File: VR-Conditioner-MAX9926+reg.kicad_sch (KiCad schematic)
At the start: 26 parts, among them J2 Edge, J3 8-pin header, U1 MAX9926UAEE+, U2 AMS1117CD-5.0

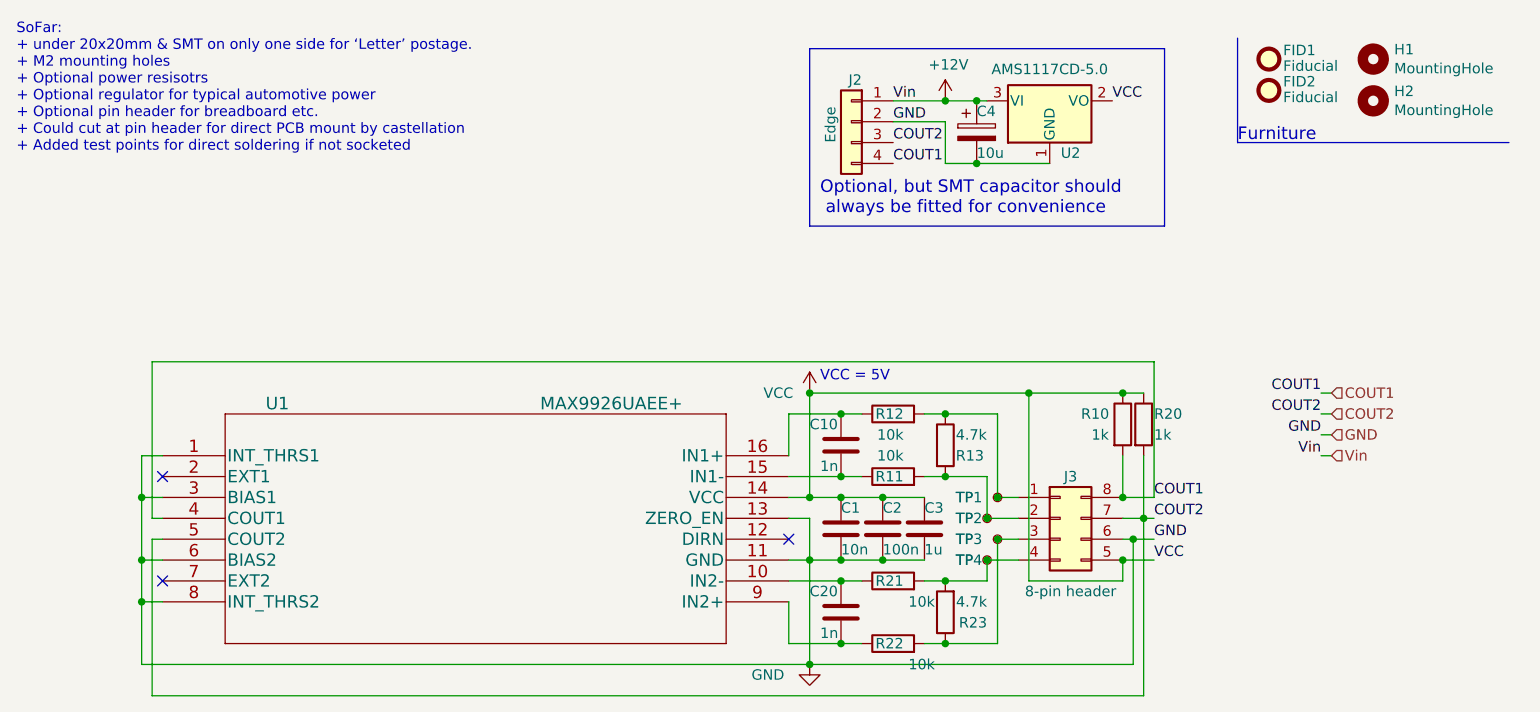
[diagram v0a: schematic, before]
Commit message: v3.74 corrects channel 1 polarity, improves silkscreen & makes soldering of PTH bits easier.
Polarity in previous version not critical as everyone seems to try their pick-up each way anyhow.
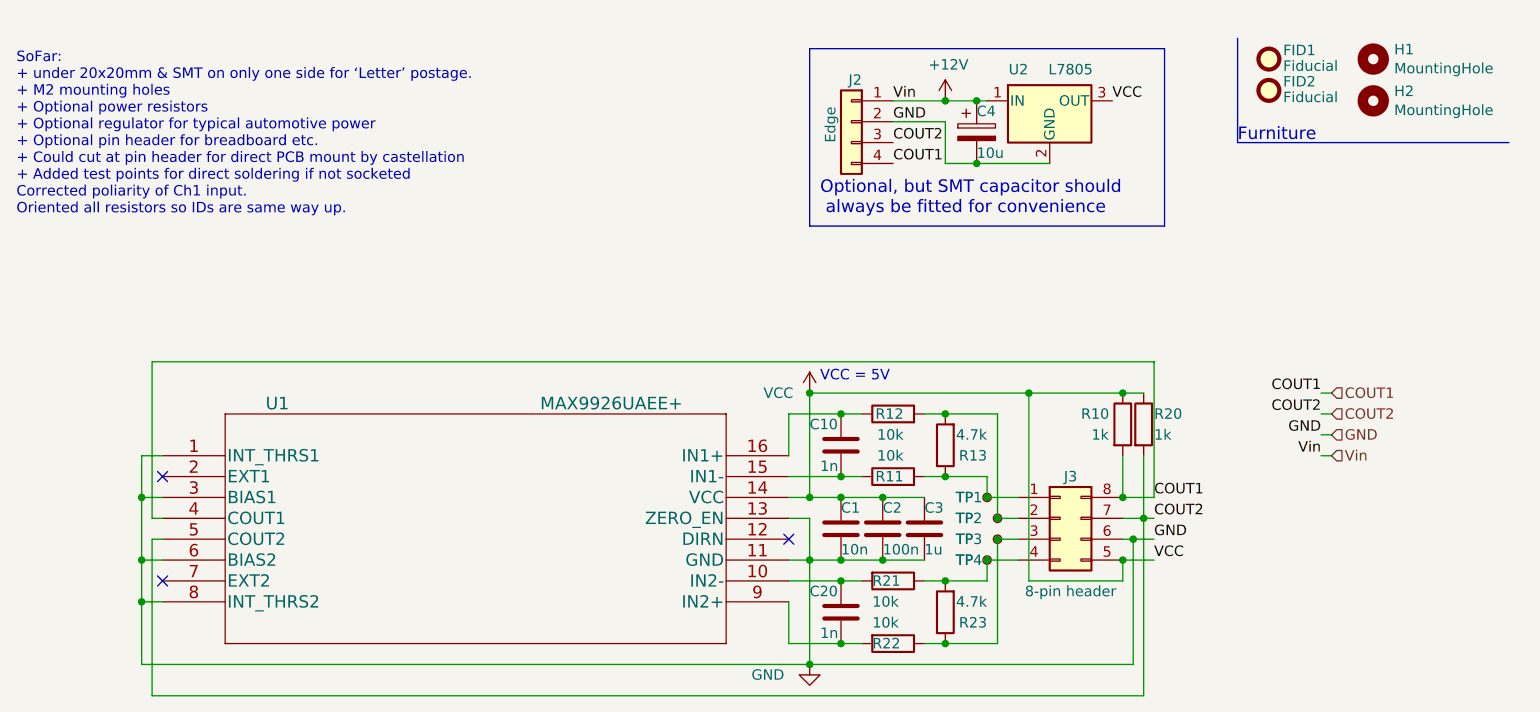
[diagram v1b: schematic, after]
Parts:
- removed U2: AMS1117CD-5.0, Package_TO_SOT_THT:TO-92_Inline_Wide, symbol Regulator_Linear:AMS1117CD-5.0
- added U2: L7805, Package_TO_SOT_THT:TO-220-3_Vertical, symbol Regulator_Linear:L7805
- R11, R12, R21, R22: footprint Resistor_SMD:R_1206_3216Metric -> Resistor_SMD:R_1206_3216Metric_Pad1.30x1.75mm_HandSolder
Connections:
- net +12V: now also U2.1 (IN)
- net GND: now also U2.2 (GND)
- net VCC: now also U2.3 (OUT)
- net at C20.1, U1.10 (IN2-): now also R21.2; no longer R21.1
- net at C20.2, U1.9 (IN2+): now also R22.2; no longer R22.1
- net at J3.1 (Pin_1), R13.1, TP1.1: now also R11.2; no longer R12.2
- net at J3.3 (Pin_3), R23.1, TP3.1: now also R22.1; no longer R22.2
- net at J3.4 (Pin_4), R23.2, TP4.1: now also R21.1; no longer R21.2
- net at J3.2 (Pin_2), R13.2, TP2.1: now also R12.2; no longer R11.2
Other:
- note added: "SoFar: + under 20x20mm & SMT on only one side for ‘Letter’ postage. + M2 mounting holes + Optional power resistors + Optional regulator for typical automotive power + Optional pin header for breadboard etc. + Could cut at pin header for direct PCB mount by castellation + Added test points for direct soldering if not socketed Corrected poliarity of Ch1 input. Oriented all resistors so IDs are same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"
- note removed: "SoFar: + under 20x20mm & SMT on only one side for ‘Letter’ postage. + M2 mounting holes + Optional power resisotrs + Optional regulator for typical automotive power + Optional pin header for breadboard etc. + Could cut at pin header for direct PCB mount by castellation + Added test points for direct soldering if not socketed"
- moved on the sheet: R13, R21, R22, TP1, TP2
